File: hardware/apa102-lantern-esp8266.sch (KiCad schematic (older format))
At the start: 17 parts, among them P1 CONN_01X02, P10 CONN_01X06, P2 CONN_01X06, P3 CONN_01X06, P4 CONN_01X06, P5 CONN_01X06, P6 CONN_01X06, P7 CONN_01X06, P8 CONN_01X06, P9 CONN_01X06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

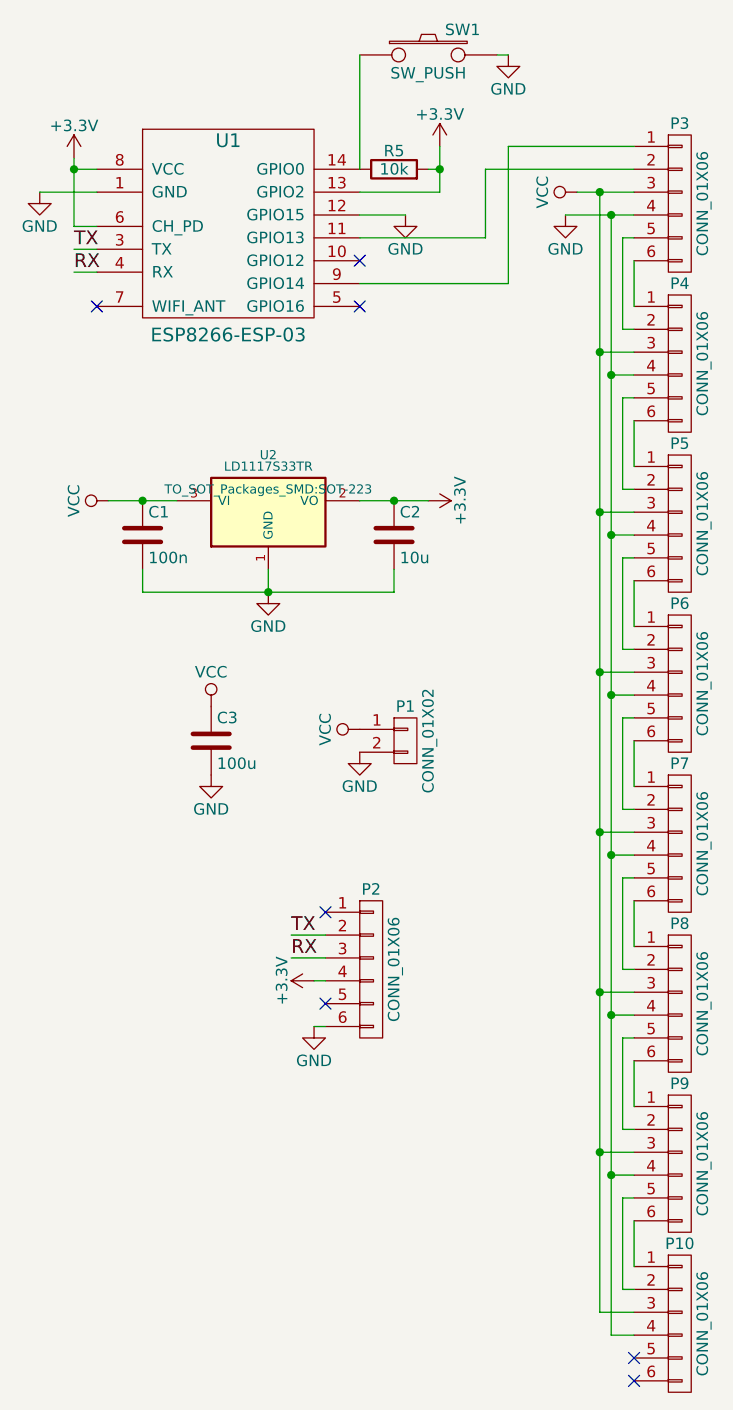
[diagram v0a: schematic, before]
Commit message: Adds pins to access the leds directly via SPI
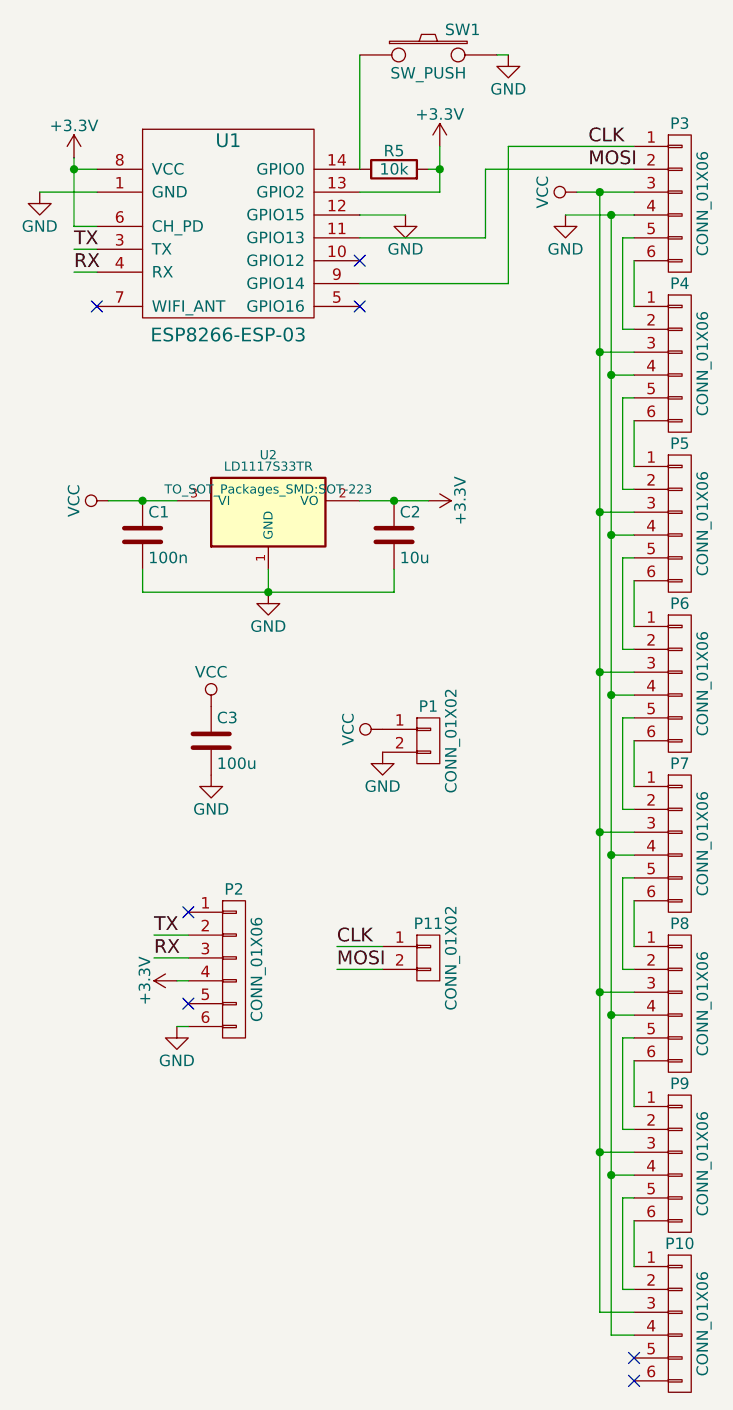
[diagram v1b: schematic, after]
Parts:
- added P11: CONN_01X02, Pin_Headers:Pin_Header_Straight_1x02, symbol CONN_01X02
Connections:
- net CLK: now reaches P3.1 (P1), U1.9 (GPIO14)
- net CLK: now also P11.1 (P1)
- net MOSI: now reaches P3.2 (P2), U1.11 (GPIO13)
- net MOSI: now also P11.2 (P2)
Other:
- moved on the sheet: P1, P2
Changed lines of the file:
@@
 L CONN_01X02 P1
 U 1 1 560CC6CB
-P 3600 4150
-F 0 "P1" H 3600 4300 50  0000 C CNN
-F 1 "CONN_01X02" V 3700 4150 50  0000 C CNN
-F 2 "Pin_Headers:Pin_Header_Straight_1x02" H 3600 4150 60  0001 C CNN
-F 3 "" H 3600 4150 60  0000 C CNN
-	1    3600 4150
+P 3700 4150
+F 0 "P1" H 3700 4300 50  0000 C CNN
+F 1 "CONN_01X02" V 3800 4150 50  0000 C CNN
+F 2 "Pin_Headers:Pin_Header_Straight_1x02" H 3700 4150 60  0001 C CNN
+F 3 "" H 3700 4150 60  0000 C CNN
+	1    3700 4150
 	1    0    0    -1
 $EndComp
@@
 L VCC #PWR08
 U 1 1 560CC7E6
-P 3400 4100
-F 0 "#PWR08" H 3400 3950 50  0001 C CNN
-F 1 "VCC" H 3400 4250 50  0000 C CNN
-F 2 "" H 3400 4100 60  0000 C CNN
-F 3 "" H 3400 4100 60  0000 C CNN
-	1    3400 4100
+P 3500 4100
+F 0 "#PWR08" H 3500 3950 50  0001 C CNN
+F 1 "VCC" H 3500 4250 50  0000 C CNN
+F 2 "" H 3500 4100 60  0000 C CNN
+F 3 "" H 3500 4100 60  0000 C CNN
+	1    3500 4100
 	0    -1   -1   0
 $EndComp
@@
 L GND #PWR09
 U 1 1 560CC84B
-P 3400 4200
-F 0 "#PWR09" H 3400 3950 50  0001 C CNN
-F 1 "GND" H 3400 4050 50  0000 C CNN
-F 2 "" H 3400 4200 60  0000 C CNN
-F 3 "" H 3400 4200 60  0000 C CNN
-	1    3400 4200
+P 3500 4200
+F 0 "#PWR09" H 3500 3950 50  0001 C CNN
+F 1 "GND" H 3500 4050 50  0000 C CNN
+F 2 "" H 3500 4200 60  0000 C CNN
+F 3 "" H 3500 4200 60  0000 C CNN
+	1    3500 4200
 	1    0    0    -1
 $EndComp
@@
 L CONN_01X06 P2
 U 1 1 560CE3F9
-P 3450 5150
-F 0 "P2" H 3450 5500 50  0000 C CNN
-F 1 "CONN_01X06" V 3550 5150 50  0000 C CNN
-F 2 "Pin_Headers:Pin_Header_Angled_1x06" H 3450 5150 60  0001 C CNN
-F 3 "" H 3450 5150 60  0000 C CNN
-	1    3450 5150
+P 2850 5150
+F 0 "P2" H 2850 5500 50  0000 C CNN
+F 1 "CONN_01X06" V 2950 5150 50  0000 C CNN
+F 2 "Pin_Headers:Pin_Header_Angled_1x06" H 2850 5150 60  0001 C CNN
+F 3 "" H 2850 5150 60  0000 C CNN
+	1    2850 5150
 	1    0    0    -1
 $EndComp
@@
 L GND #PWR013
 U 1 1 560CE8EA
-P 3200 5400
-F 0 "#PWR013" H 3200 5150 50  0001 C CNN
-F 1 "GND" H 3200 5250 50  0000 C CNN
-F 2 "" H 3200 5400 60  0000 C CNN
-F 3 "" H 3200 5400 60  0000 C CNN
-	1    3200 5400
-	1    0    0    -1
-$EndComp
-Wire Wire Line
-	3200 5400 3250 5400
-Wire Wire Line
-	3100 5000 3250 5000
-Wire Wire Line
-	3100 5100 3250 5100
+P 2600 5400
+F 0 "#PWR013" H 2600 5150 50  0001 C CNN
+F 1 "GND" H 2600 5250 50  0000 C CNN
+F 2 "" H 2600 5400 60  0000 C CNN
+F 3 "" H 2600 5400 60  0000 C CNN
+	1    2600 5400
+	1    0    0    -1
+$EndComp
+Wire Wire Line
+	2600 5400 2650 5400
+Wire Wire Line
+	2500 5000 2650 5000
+Wire Wire Line
+	2500 5100 2650 5100
 $Comp
 L +3.3V #PWR014
 U 1 1 560CEC9A
-P 3200 5200
-F 0 "#PWR014" H 3200 5050 50  0001 C CNN
-F 1 "+3.3V" H 3200 5340 50  0000 C CNN
-F 2 "" H 3200 5200 60  0000 C CNN
-F 3 "" H 3200 5200 60  0000 C CNN
-	1    3200 5200
+P 2600 5200
+F 0 "#PWR014" H 2600 5050 50  0001 C CNN
+F 1 "+3.3V" H 2600 5340 50  0000 C CNN
+F 2 "" H 2600 5200 60  0000 C CNN
+F 3 "" H 2600 5200 60  0000 C CNN
+	1    2600 5200
 	0    -1   -1   0
 $EndComp
 Wire Wire Line
-	3200 5200 3250 5200
-Text Label 3100 5100 0    60   ~ 0
+	2600 5200 2650 5200
+Text Label 2500 5100 0    60   ~ 0
 RX
-Text Label 3100 5000 0    60   ~ 0
+Text Label 2500 5000 0    60   ~ 0
 TX
 Wire Wire Line
@@
 Wire Wire Line
 	4000 1150 4050 1150
-NoConn ~ 3250 5300
-NoConn ~ 3250 4900
+NoConn ~ 2650 5300
+NoConn ~ 2650 4900
 $Comp
 L CONN_01X06 P9
@@
 Wire Wire Line
 	3950 1650 4600 1650
+$Comp
+L CONN_01X02 P11
+U 1 1 561125AA
+P 3700 5100
+F 0 "P11" H 3700 5250 50  0000 C CNN
+F 1 "CONN_01X02" V 3800 5100 50  0000 C CNN
+F 2 "Pin_Headers:Pin_Header_Straight_1x02" H 3700 5100 60  0001 C CNN
+F 3 "" H 3700 5100 60  0000 C CNN
+	1    3700 5100
+	1    0    0    -1
+$EndComp
+Text Label 4400 1550 0    60   ~ 0
+CLK
+Text Label 4400 1650 0    60   ~ 0
+MOSI
+Text Label 3300 5050 0    60   ~ 0
+CLK
+Text Label 3300 5150 0    60   ~ 0
+MOSI
+Wire Wire Line
+	3300 5050 3500 5050
+Wire Wire Line
+	3500 5150 3300 5150
 $EndSCHEMATC

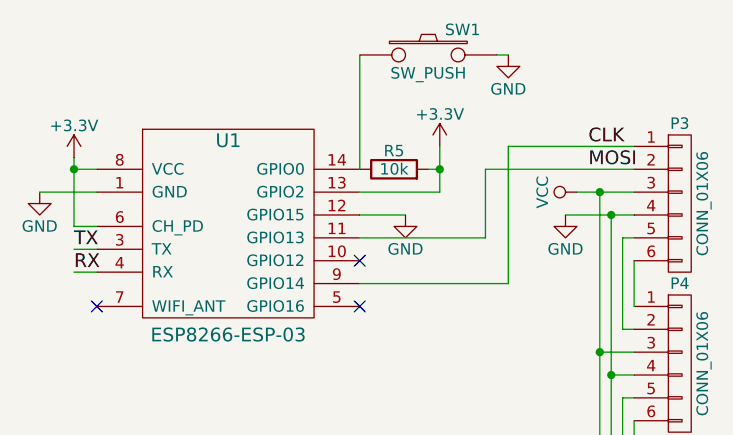
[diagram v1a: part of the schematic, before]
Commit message: Silkscreen fixes
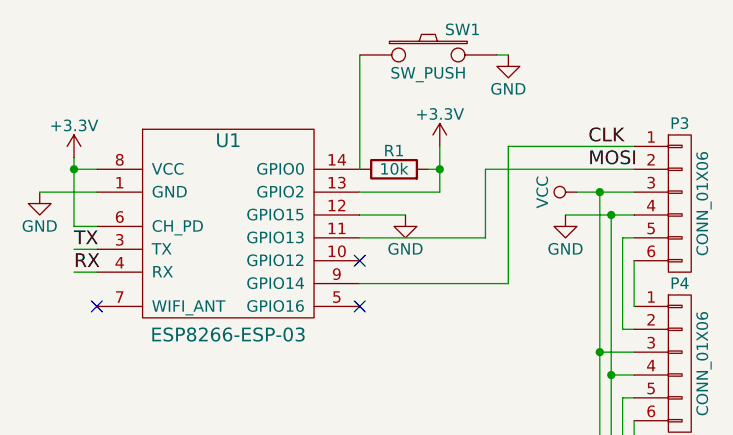
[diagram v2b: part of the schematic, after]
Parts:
- renumbered R5 to R1
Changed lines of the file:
@@
 $EndComp
 $Comp
-L R R5
+L R R1
 U 1 1 560CDE16
 P 3550 1650
-F 0 "R5" V 3630 1650 50  0000 C CNN
+F 0 "R1" V 3630 1650 50  0000 C CNN
 F 1 "10k" V 3550 1650 50  0000 C CNN
 F 2 "Resistors_SMD:R_0603_HandSoldering" V 3480 1650 30  0001 C CNN
